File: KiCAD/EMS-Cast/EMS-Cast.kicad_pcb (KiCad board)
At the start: 2 copper layers, 107.5 x 78.5 mm, 42 parts, among them IC1 LH1546ADF, IC2 LH1546ADF, IC3 LH1546ADF, IC4 LH1546ADF, J1 1720430202, J2 5-103166-1, J3 5-103166-1, Q1 STD25NF20, Q2 STD25NF20, Q3 STD25NF20, Q4 STD25NF20, SW2 SW_Push, SW3 SW_Push, U1 AD5252BRUZ10-RL7, U2 VOM1271T, U3 VOM1271T, U4 KF80BDT

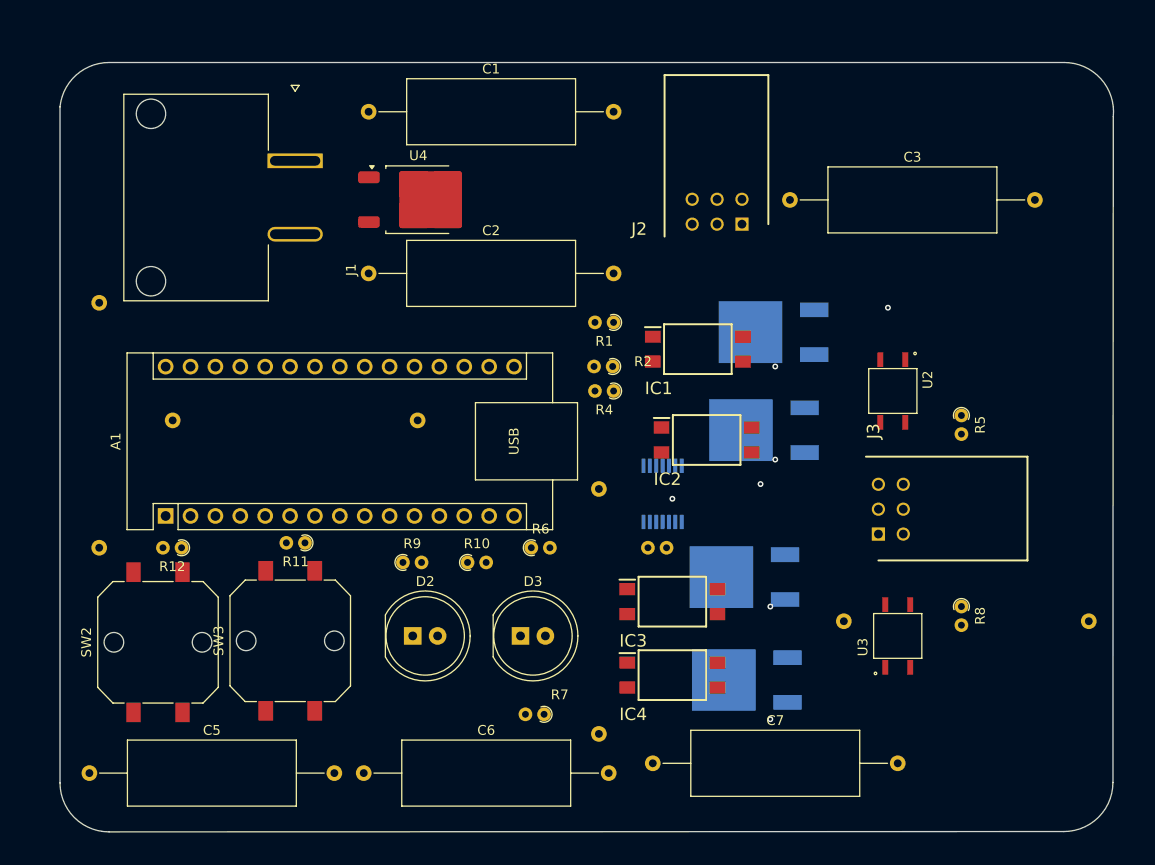
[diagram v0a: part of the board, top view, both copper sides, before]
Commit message: Multiple Changes
- Updated KICAD for proposal images
- Added Arduino code folder with basic .ino code (basic requirement and temporary pin mappings)
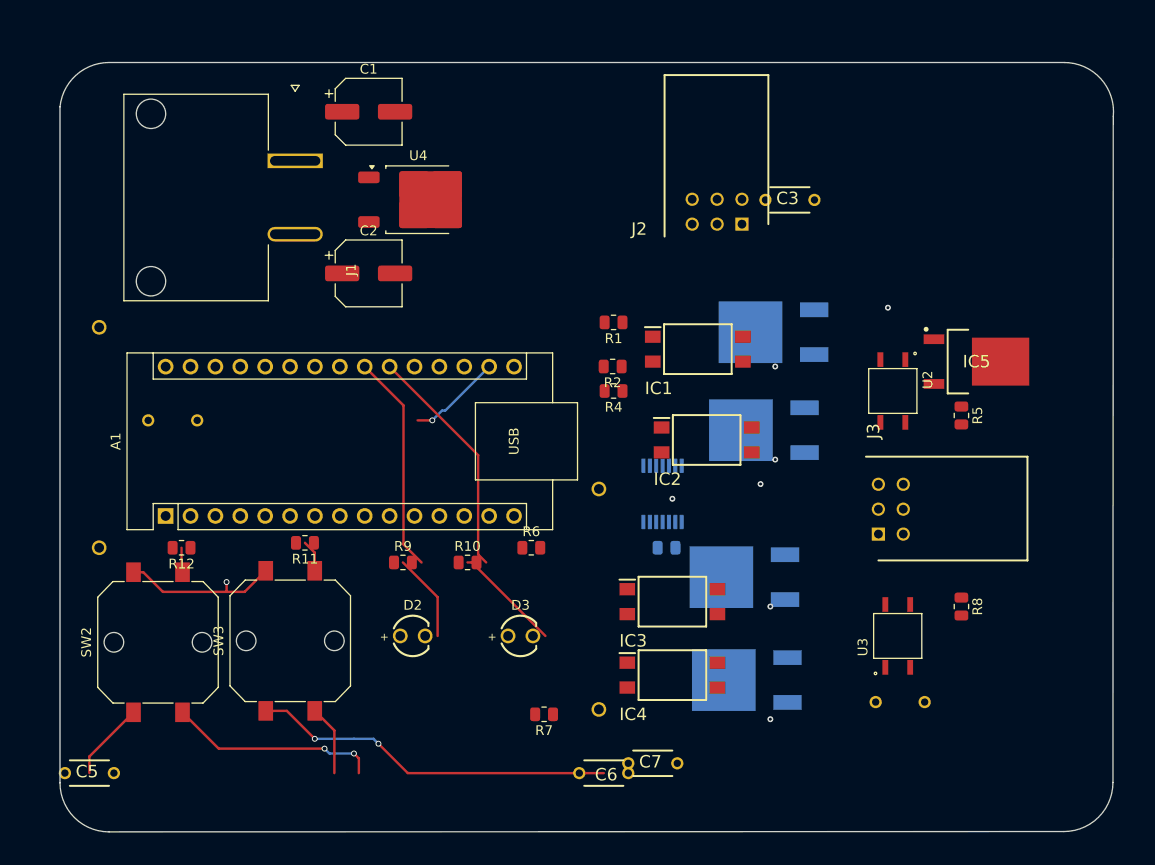
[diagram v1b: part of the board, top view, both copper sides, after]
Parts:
- added IC5: KF33BDT-TR, EMS_lib:TO228P972X240-3N, F.Cu at (184.6, 77.0)
- C1, C2: footprint Capacitor_THT:C_Axial_L17.0mm_D6.5mm_P25.00mm_Horizontal -> Capacitor_SMD:CP_Elec_6.3x3
- C10, C9: footprint Capacitor_THT:C_Axial_L17.0mm_D6.5mm_P25.00mm_Horizontal -> EMS_lib:ECQE4105KF
- C3, C4, C5, C6, C7, C8: footprint Capacitor_THT:C_Axial_L17.0mm_D6.5mm_P25.00mm_Horizontal -> EMS_lib:K104K15X7RF53H5
- D2, D3: footprint LED_THT:LED_D8.0mm -> EMS_lib:WL-TMRC_3MM
- R1, R10, R11, R12, R2, R3, R4, R5, R6, R7, R8, R9: footprint Resistor_THT:R_Axial_DIN0204_L3.6mm_D1.6mm_P1.90mm_Vertical -> Resistor_SMD:R_0805_2012Metric
- moved C6 24.5 mm to (146.5, 119.0), turned to 180 degrees
- moved C4 20.9 mm to (176.8, 111.8), turned to 0 degrees
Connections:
- C1 pad 1: Net-(U4-VI) -> Net-(IC5-INPUT)
- J1 pad 1: Net-(U4-VI) -> Net-(IC5-INPUT)
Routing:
- net GND: track 0.00 -> 61.4 mm, vias 3 -> 6
- net Net-(A1-A2): track 0.00 -> 35.1 mm
- net Net-(A1-A3): track 0.00 -> 31.4 mm
- net /SW_CH1: track 0.00 -> 24.0 mm, vias 0 -> 2
- net /SW_CH2: track 0.00 -> 10.4 mm
- net +3.3V: track 0.00 -> 9.57 mm, vias 0 -> 1
